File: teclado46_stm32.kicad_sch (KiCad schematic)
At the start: 0 parts

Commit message: chore: label stm32g474
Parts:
- added C1, C14, C2: 1u, Capacitor_SMD:C_0402_1005Metric, symbol Device:C_Small
- added C3: 10u, Capacitor_SMD:C_0603_1608Metric, symbol Device:C_Small
- added C4, C5, C6, C7: 100n, Capacitor_SMD:C_0402_1005Metric, symbol Device:C_Small
- added U1: XC6206PxxxMR, Package_TO_SOT_SMD:SOT-23-3, symbol Regulator_Linear:XC6206PxxxMR
- added U2: STM32G474CETx, Package_QFP:LQFP-48_7x7mm_P0.5mm, symbol MCU_ST_STM32G4:STM32G474CETx
- added U4: W25Q128JVS, Package_SO:SOIC-8_5.3x5.3mm_P1.27mm, symbol Memory_Flash:W25Q128JVS
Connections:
- new net +3.3V: C3.1, C4.1, C5.1, C6.1, C7.1, U2.21 (VDDA), U2.24 (VDD), U2.36 (VDD), U2.48 (VDD)
- new net +3V3: C14.1, C2.1, U1.2 (VO), U4.8 (VCC)
- new net +5V: C1.1, U1.3 (VI)
- new net BOOT0: U2.45 (PB8)
- new net D+: U2.34 (PA12)
- new net D-: U2.33 (PA11)
- new net GND: C1.2, C14.2, C2.2, C3.2, C4.2, C5.2, C6.2, C7.2, U1.1 (GND), U2.19 (VSSA), U2.23 (VSS), U2.35 (VSS), U2.47 (VSS), U4.4 (GND)
- new net NRST: U2.7 (PG10)
- new net Q_100: U2.17 (PB1), U4.5 (DI/IO_{0})
- new net Q_101: U2.16 (PB0), U4.2 (DO/IO_{1})
- new net Q_102: U2.15 (PA7), U4.3 (~{WP}/IO_{2})
- new net Q_103: U2.14 (PA6), U4.7 (~{HOLD}/~{RESET}/IO_{3})
- new net Q_CLK: U2.22 (PB10), U4.6 (CLK)
- new net Q_SEL: U2.25 (PB11), U4.1 (~{CS})

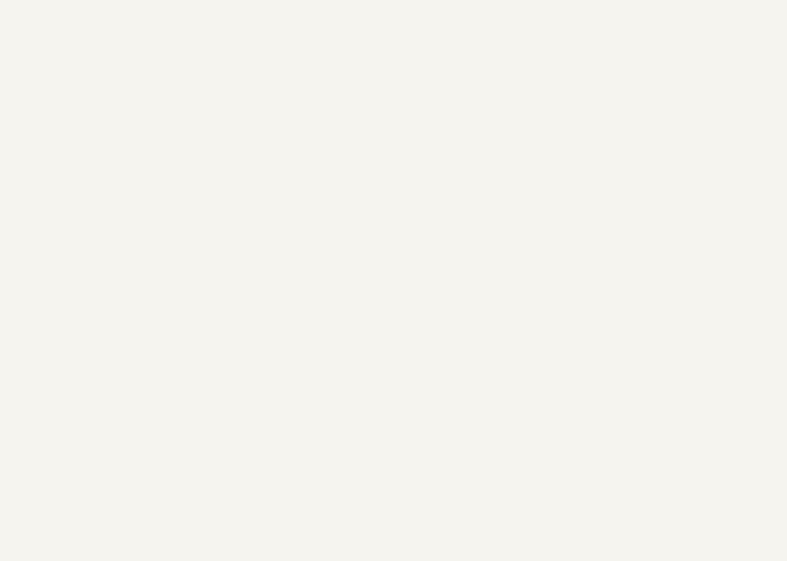
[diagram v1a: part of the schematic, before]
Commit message: chore: add keyboard switches
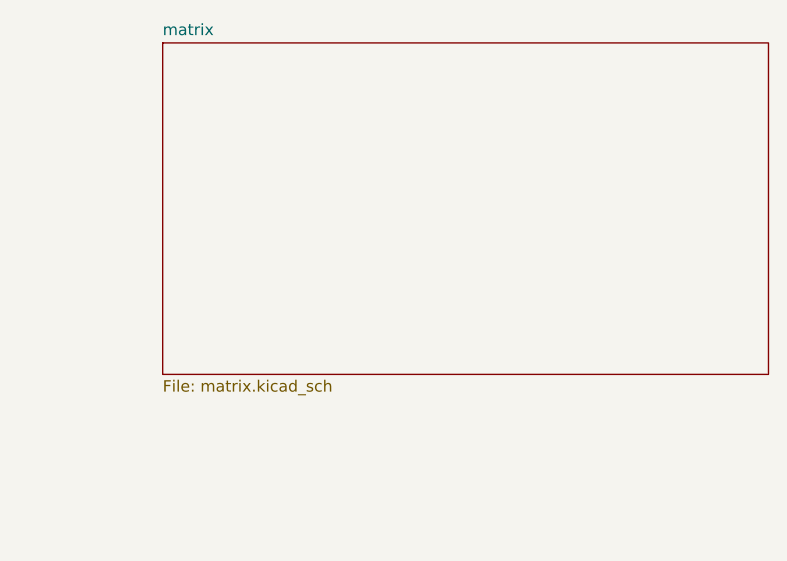
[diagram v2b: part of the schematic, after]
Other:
- added sheet matrix (matrix.kicad_sch)
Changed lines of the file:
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@@
+		)
+	)
+	(sheet
+		(at 210.82 19.05)
+		(size 67.31 36.83)
+		(exclude_from_sim no)
+		(in_bom yes)
+		(on_board yes)
+		(dnp no)
+		(fields_autoplaced yes)
+		(stroke
+			(width 0.1524)
+			(type solid)
+		)
+		(fill
+			(color 0 0 0 0.0000)
+		)
+		(property "Sheetname" "matrix"
+			(at 210.82 18.3384 0)
+			(effects
+				(font
+					(size 1.27 1.27)
+				)
+				(justify left bottom)
+			)
+		)
+		(property "Sheetfile" "matrix.kicad_sch"
+			(at 210.82 56.4646 0)
+			(effects
+				(font
+					(size 1.27 1.27)
+				)
+				(justify left top)
+			)
+		)
+		(instances
+			(project "teclado46_stm32"
+				(path "/6ed4739c-92e8-425a-abb0-74006c04cb3a"
+					(page "2")
+				)
+			)
 		)
 	)

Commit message: chore: routed caps, flash and regulator
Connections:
- net +3.3V is gone; now on net +3V3: C3.1, C4.1, C5.1, C6.1, C7.1, U2.21 (VDDA), U2.24 (VDD), U2.36 (VDD), U2.48 (VDD)
- net Q_CLK: now also U2.11 (PA3)
- net Q_SEL: now also U2.10 (PA2)
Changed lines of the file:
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@@
+	)
+	(junction
+		(at 55.88 102.87)
+		(diameter 0)
+		(color 0 0 0 0)
 	)
 	(junction
@@
 	)
 	(junction
-		(at 55.88 102.87)
-		(diameter 0)
-		(color 0 0 0 0)
-	)
-	(junction
 		(at 156.21 140.97)
 		(diameter 0)
@@
 	(wire
 		(pts
-			(xy 55.88 100.33) (xy 55.88 102.87)
-		)
-		(stroke
-			(width 0)
-			(type default)
-		)
-	)
-	(wire
-		(pts
 			(xy 128.27 143.51) (xy 128.27 140.97)
 		)
@@
 	(wire
 		(pts
+			(xy 55.88 97.79) (xy 55.88 102.87)
+		)
+		(stroke
+			(width 0)
+			(type default)
+		)
+	)
+	(wire
+		(pts
 			(xy 128.27 140.97) (xy 135.89 140.97)
 		)
@@
 	(wire
 		(pts
-			(xy 128.27 133.35) (xy 128.27 135.89)
-		)
-		(stroke
-			(width 0)
-			(type default)
-		)
-	)
-	(wire
-		(pts
 			(xy 132.08 104.14) (xy 132.08 107.95)
 		)
@@
 			(width 0)
 			(type default)
+		)
+	)
+	(global_label "Q_SEL"
+		(shape input)
+		(at 68.58 115.57 0)
+		(fields_autoplaced yes)
+		(effects
+			(font
+				(size 1.27 1.27)
+			)
+			(justify left)
+		)
+		(property "Intersheetrefs" "${INTERSHEET_REFS}"
+			(at 77.2499 115.57 0)
+			(effects
+				(font
+					(size 1.27 1.27)
+				)
+				(justify left)
+				(hide yes)
+			)
 		)
 	)
@@
 				)
 				(justify right)
+				(hide yes)
+			)
+		)
+	)
+	(global_label "Q_CLK"
+		(shape input)
+		(at 68.58 118.11 0)
+		(fields_autoplaced yes)
+		(effects
+			(font
+				(size 1.27 1.27)
+			)
+			(justify left)
+		)
+		(property "Intersheetrefs" "${INTERSHEET_REFS}"
+			(at 77.4314 118.11 0)
+			(effects
+				(font
+					(size 1.27 1.27)
+				)
+				(justify left)
 				(hide yes)
 			)
@@
 	)
 	(symbol
+		(lib_id "power:+3V3")
+		(at 128.27 135.89 0)
+		(unit 1)
+		(exclude_from_sim no)
+		(in_bom yes)
+		(on_board yes)
+		(dnp no)
+		(fields_autoplaced yes)
+		(property "Reference" "#PWR05"
+			(at 128.27 139.7 0)
+			(effects
+				(font
+					(size 1.27 1.27)
+				)
+				(hide yes)
+			)
+		)
+		(property "Value" "+3V3"
+			(at 128.27 130.81 0)
+			(effects
+				(font
+					(size 1.27 1.27)
+				)
+			)
+		)
+		(property "Footprint" ""
+			(at 128.27 135.89 0)
+			(effects
+				(font
+					(size 1.27 1.27)
+				)
+				(hide yes)
+			)
+		)
+		(property "Datasheet" ""
+			(at 128.27 135.89 0)
+			(effects
+				(font
+					(size 1.27 1.27)
+				)
+				(hide yes)
+			)
+		)
+		(property "Description" "Power symbol creates a global label with name \"+3V3\""
+			(at 128.27 135.89 0)
+			(effects
+				(font
+					(size 1.27 1.27)
+				)
+				(hide yes)
+			)
+		)
+		(pin "1"
+		)
+		(instances
+			(project "teclado46_stm32"
+				(path "/6ed4739c-92e8-425a-abb0-74006c04cb3a"
+					(reference "#PWR05")
+					(unit 1)
+				)
+			)
+		)
+	)
+	(symbol
 		(lib_id "power:GND")
 		(at 128.27 143.51 0)
@@
 	)
 	(symbol
-		(lib_id "power:+3.3V")
-		(at 55.88 100.33 0)
-		(unit 1)
-		(exclude_from_sim no)
-		(in_bom yes)
-		(on_board yes)
-		(dnp no)
-		(fields_autoplaced yes)
-		(property "Reference" "#PWR03"
-			(at 55.88 104.14 0)
-			(effects
-				(font
-					(size 1.27 1.27)
-				)
-				(hide yes)
-			)
-		)
-		(property "Value" "+3.3V"
-			(at 55.88 95.25 0)
-			(effects
-				(font
-					(size 1.27 1.27)
-				)
-			)
-		)
-		(property "Footprint" ""
-			(at 55.88 100.33 0)
-			(effects
-				(font
-					(size 1.27 1.27)
-				)
-				(hide yes)
-			)
-		)
-		(property "Datasheet" ""
-			(at 55.88 100.33 0)
-			(effects
-				(font
-					(size 1.27 1.27)
-				)
-				(hide yes)
-			)
-		)
-		(property "Description" "Power symbol creates a global label with name \"+3.3V\""
-			(at 55.88 100.33 0)
-			(effects
-				(font
-					(size 1.27 1.27)
-				)
-				(hide yes)
-			)
-		)
-		(pin "1"
-		)
-		(instances
-			(project ""
-				(path "/6ed4739c-92e8-425a-abb0-74006c04cb3a"
-					(reference "#PWR03")
-					(unit 1)
-				)
-			)
-		)
-	)
-	(symbol
 		(lib_id "power:+5V")
 		(at 129.54 99.06 0)
@@
 	)
 	(symbol
-		(lib_id "power:+3.3V")
-		(at 128.27 133.35 0)
+		(lib_id "power:+3V3")
+		(at 55.88 97.79 0)
 		(unit 1)
 		(exclude_from_sim no)
@@
 		(dnp no)
 		(fields_autoplaced yes)
-		(property "Reference" "#PWR05"
-			(at 128.27 137.16 0)
-			(effects
-				(font
-					(size 1.27 1.27)
-				)
-				(hide yes)
-			)
-		)
-		(property "Value" "+3.3V"
-			(at 128.27 128.27 0)
+		(property "Reference" "#PWR03"
+			(at 55.88 101.6 0)
+			(effects
+				(font
+					(size 1.27 1.27)
+				)
+				(hide yes)
+			)
+		)
+		(property "Value" "+3V3"
+			(at 55.88 92.71 0)
 			(effects
 				(font
@@
 		)
 		(property "Footprint" ""
-			(at 128.27 133.35 0)
+			(at 55.88 97.79 0)
 			(effects
 				(font
@@
 		)
 		(property "Datasheet" ""
-			(at 128.27 133.35 0)
-			(effects
-				(font
-					(size 1.27 1.27)
-				)
-				(hide yes)
-			)
-		)
-		(property "Description" "Power symbol creates a global label with name \"+3.3V\""
-			(at 128.27 133.35 0)
+			(at 55.88 97.79 0)
+			(effects
+				(font
+					(size 1.27 1.27)
+				)
+				(hide yes)
+			)
+		)
+		(property "Description" "Power symbol creates a global label with name \"+3V3\""
+			(at 55.88 97.79 0)
 			(effects
 				(font
@@
 			(project "teclado46_stm32"
 				(path "/6ed4739c-92e8-425a-abb0-74006c04cb3a"
-					(reference "#PWR05")
+					(reference "#PWR03")
 					(unit 1)
 				)

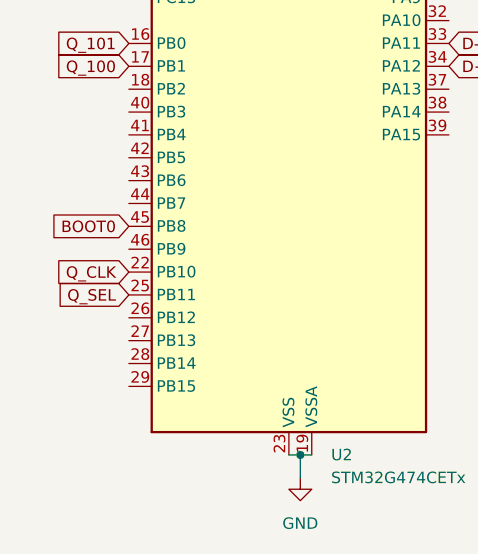
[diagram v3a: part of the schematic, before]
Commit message: chore: disconnect a Q_CLK and Q_SEL pin
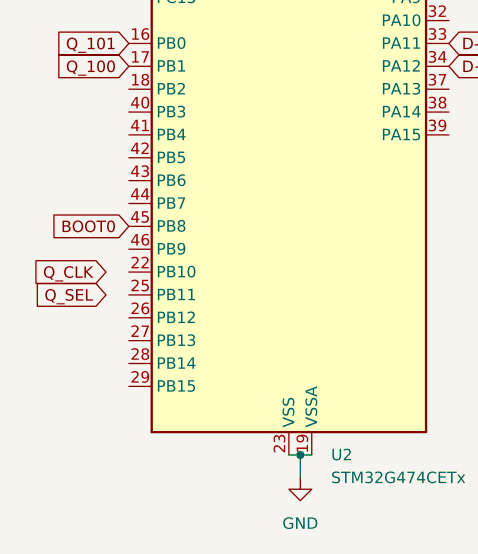
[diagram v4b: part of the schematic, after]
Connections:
- net Q_CLK: no longer U2.22 (PB10)
- net Q_SEL: no longer U2.25 (PB11)
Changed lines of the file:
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@@
 	(global_label "Q_CLK"
 		(shape input)
-		(at 33.02 163.83 180)
+		(at 30.48 163.83 180)
 		(fields_autoplaced yes)
 		(effects
@@
 		)
 		(property "Intersheetrefs" "${INTERSHEET_REFS}"
-			(at 24.1686 163.83 0)
+			(at 21.6286 163.83 0)
 			(effects
 				(font
@@
 	(global_label "Q_SEL"
 		(shape input)
-		(at 33.02 166.37 180)
+		(at 30.48 166.37 180)
 		(fields_autoplaced yes)
 		(effects
@@
 		)
 		(property "Intersheetrefs" "${INTERSHEET_REFS}"
-			(at 24.3501 166.37 0)
+			(at 21.8101 166.37 0)
 			(effects
 				(font

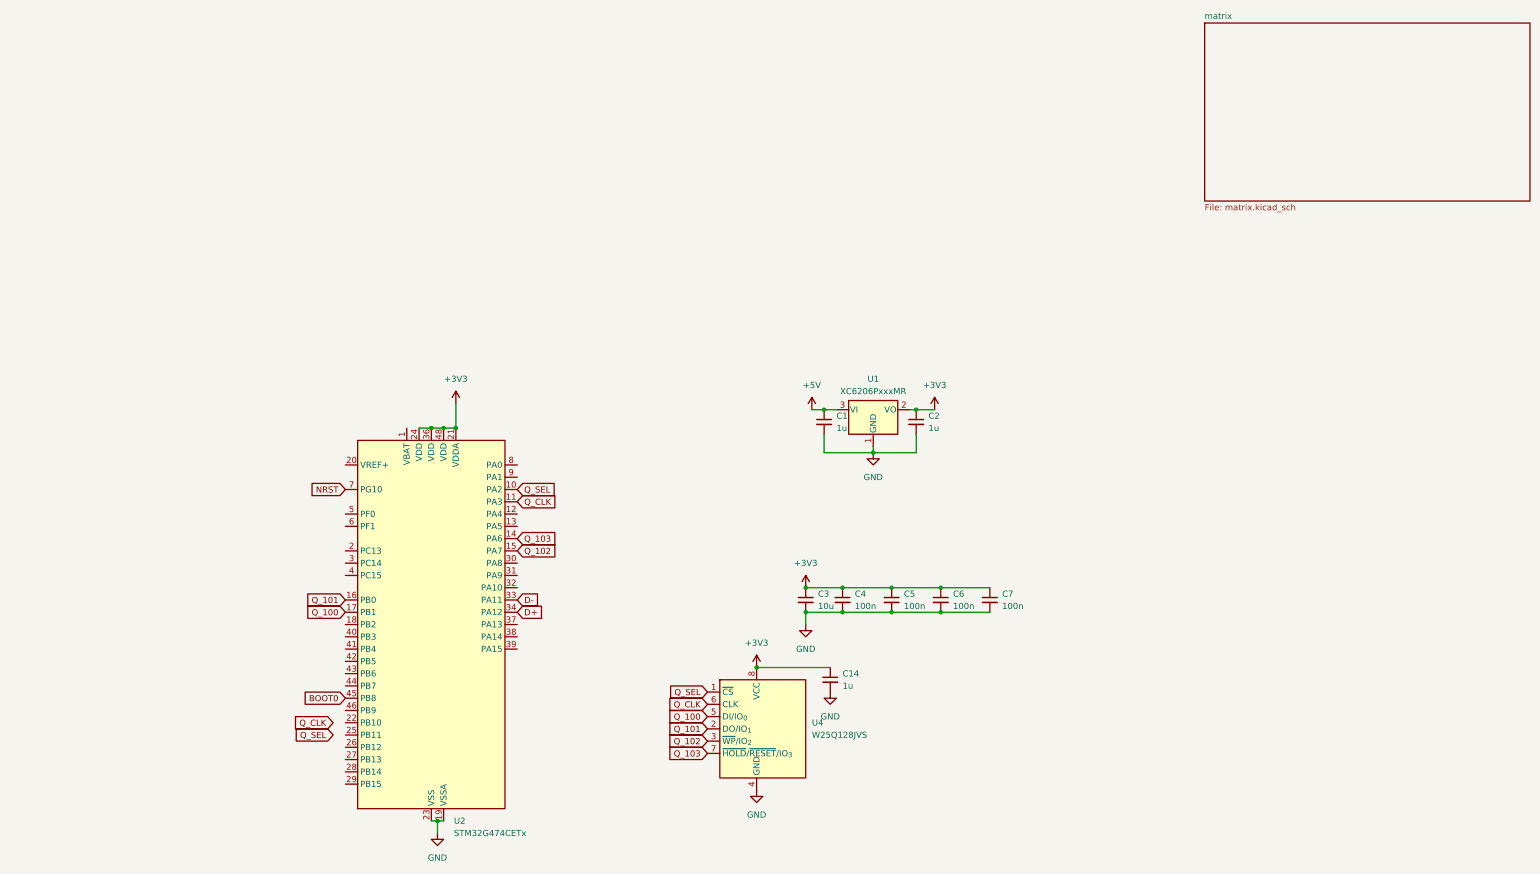
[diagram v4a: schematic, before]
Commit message: chore: add udb connector to schem
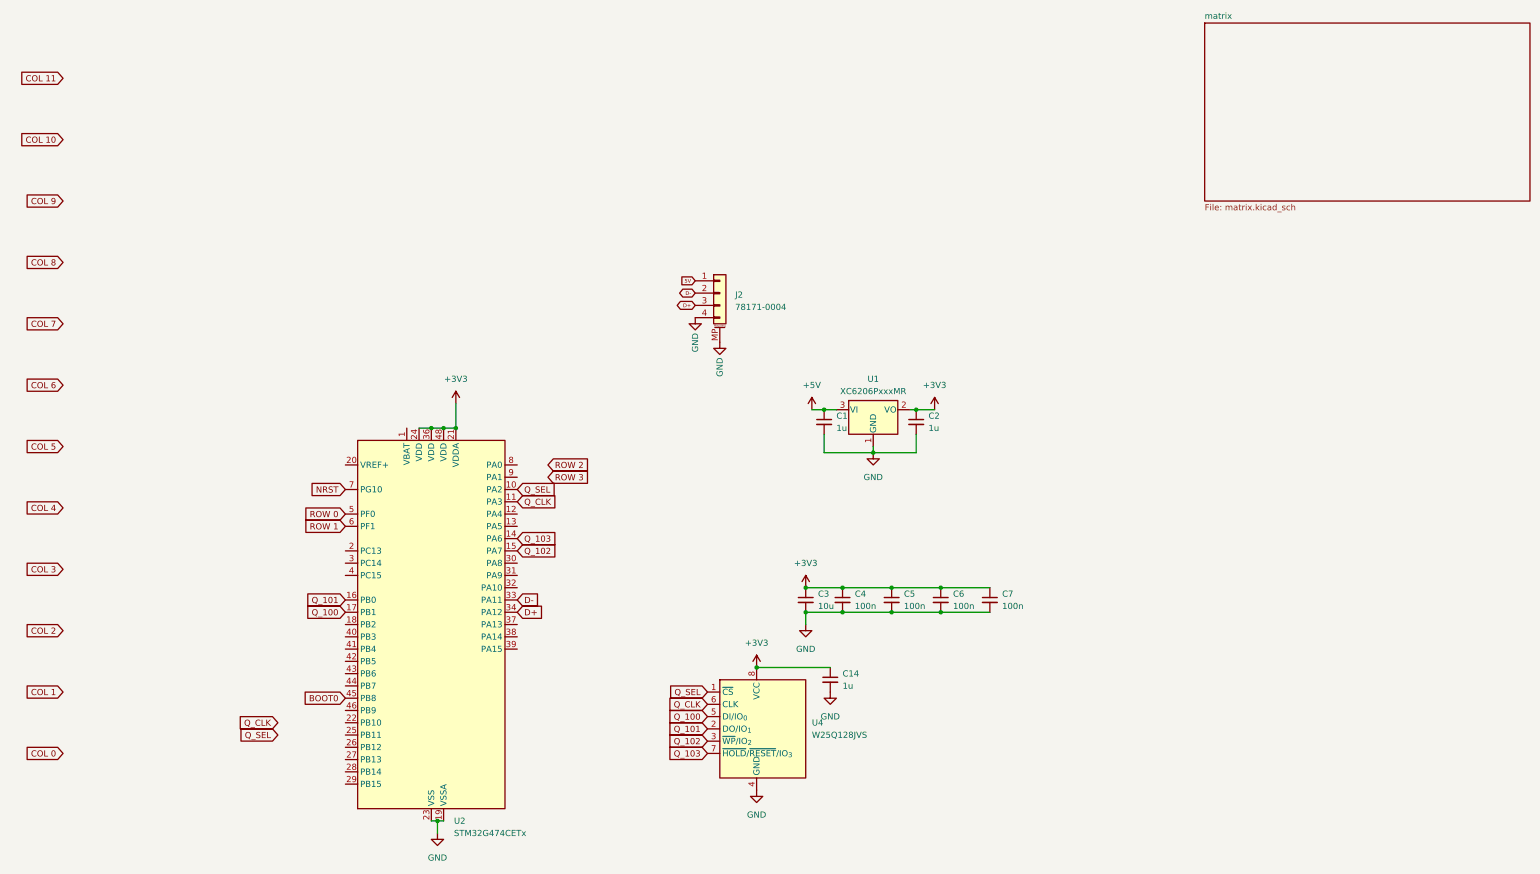
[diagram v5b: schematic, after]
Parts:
- added J2: 78171-0004, locallib:PicoEZMate-Reinforced-Lite, symbol Connector_Generic_MountingPin:Conn_01x04_MountingPin
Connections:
- net D+: now also J2.3 (Pin_3)
- net D-: now also J2.2 (Pin_2)
- net GND: now also J2.4 (Pin_4), J2.MP (MountPin)
- net ROW 0: now reaches U2.5 (PF0)
- net ROW 1: now reaches U2.6 (PF1)
- new net 5V: J2.1 (Pin_1)

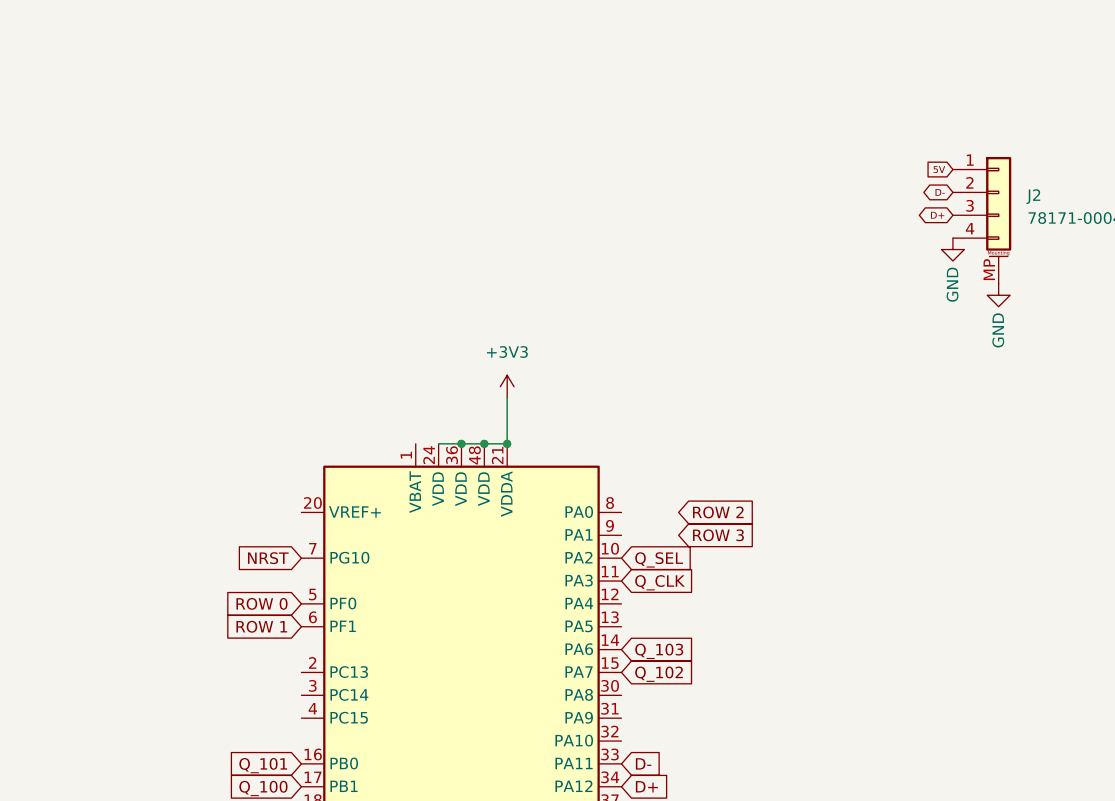
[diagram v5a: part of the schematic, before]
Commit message: chore: wired udb connector
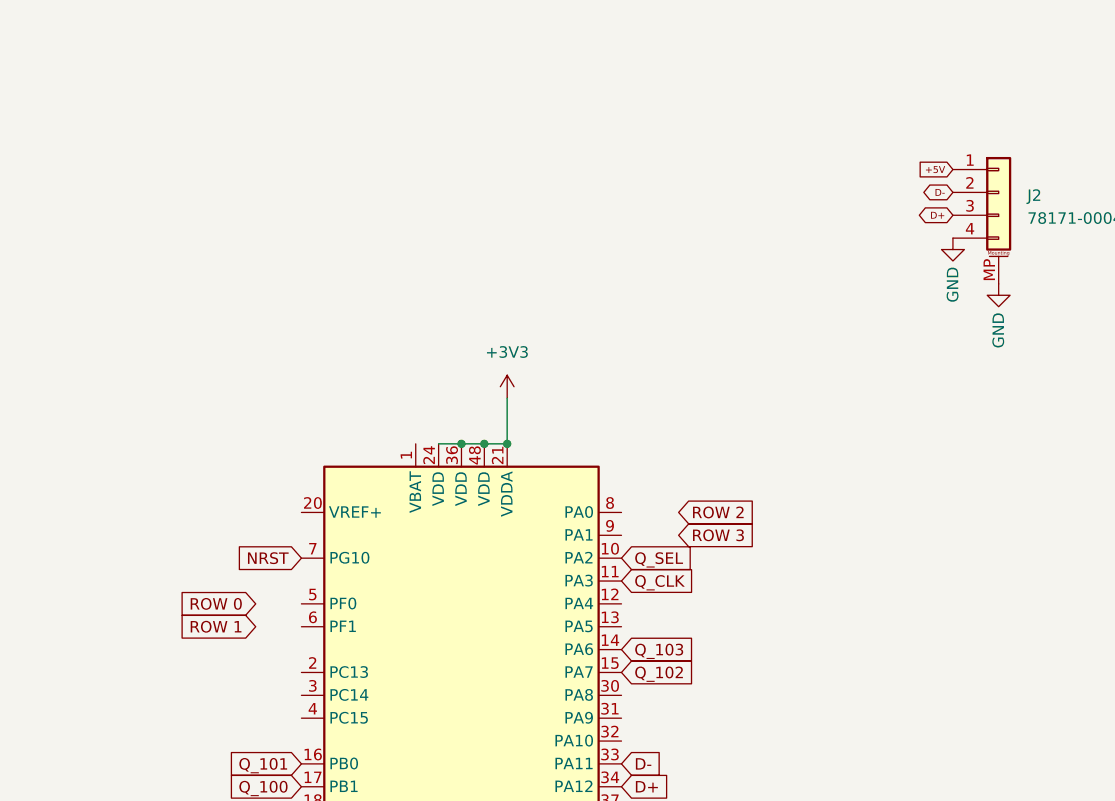
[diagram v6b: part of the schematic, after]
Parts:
- J2: footprint locallib:PicoEZMate-Reinforced-Lite -> PCM_marbastlib-various:Molex_Pico-EZmate_78171-0004_1x04-1MP_P1.20mm_Vertical
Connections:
- net 5V is gone; now on net +5V: J2.1 (Pin_1)
- net ROW 0: no longer U2.5 (PF0)
- net ROW 1: no longer U2.6 (PF1)
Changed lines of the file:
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@@
 	(global_label "ROW 1"
 		(shape input)
-		(at 33.02 123.19 180)
-		(fields_autoplaced yes)
-		(effects
-			(font
-				(size 1.27 1.27)
-			)
-			(justify right)
-		)
-		(property "Intersheetrefs" "${INTERSHEET_REFS}"
-			(at 23.8058 123.19 0)
+		(at 27.94 123.19 180)
+		(fields_autoplaced yes)
+		(effects
+			(font
+				(size 1.27 1.27)
+			)
+			(justify right)
+		)
+		(property "Intersheetrefs" "${INTERSHEET_REFS}"
+			(at 18.7258 123.19 0)
 			(effects
 				(font
@@
 	(global_label "ROW 0"
 		(shape input)
-		(at 33.02 120.65 180)
-		(fields_autoplaced yes)
-		(effects
-			(font
-				(size 1.27 1.27)
-			)
-			(justify right)
-		)
-		(property "Intersheetrefs" "${INTERSHEET_REFS}"
-			(at 23.8058 120.65 0)
+		(at 27.94 120.65 180)
+		(fields_autoplaced yes)
+		(effects
+			(font
+				(size 1.27 1.27)
+			)
+			(justify right)
+		)
+		(property "Intersheetrefs" "${INTERSHEET_REFS}"
+			(at 18.7258 120.65 0)
 			(effects
 				(font
@@
 		)
 	)
-	(global_label "5V"
+	(global_label "+5V"
 		(shape input)
 		(at 105.41 72.39 180)
@@
 		)
 		(property "Intersheetrefs" "${INTERSHEET_REFS}"
-			(at 102.5832 72.3424 0)
+			(at 101.2964 72.39 0)
 			(effects
 				(font
@@
 			)
 		)
-		(property "Footprint" "locallib:PicoEZMate-Reinforced-Lite"
+		(property "Footprint" "PCM_marbastlib-various:Molex_Pico-EZmate_78171-0004_1x04-1MP_P1.20mm_Vertical"
 			(at 110.49 74.93 0)
 			(effects
